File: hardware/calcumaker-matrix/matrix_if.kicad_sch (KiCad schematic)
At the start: 1 part, among them J1 TO MCU (unified SPI FFC)

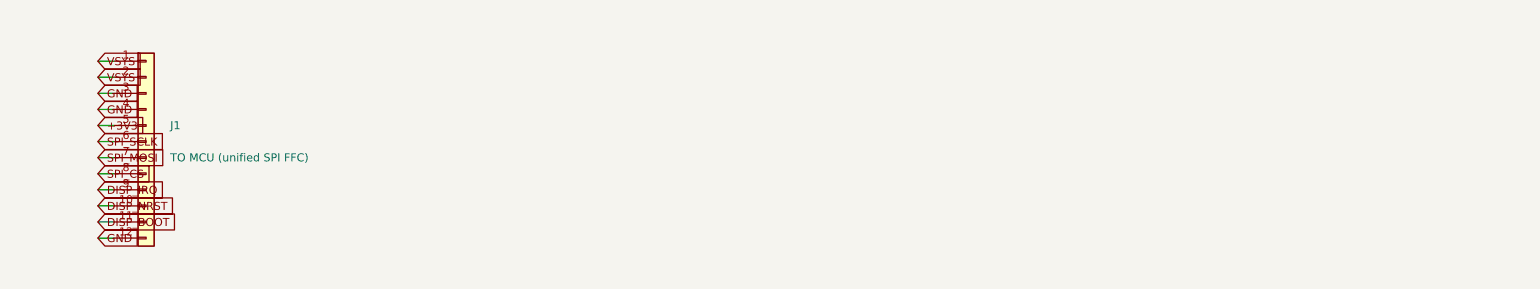
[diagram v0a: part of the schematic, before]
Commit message: Floorplan both display PCBs and verify their schematic nets
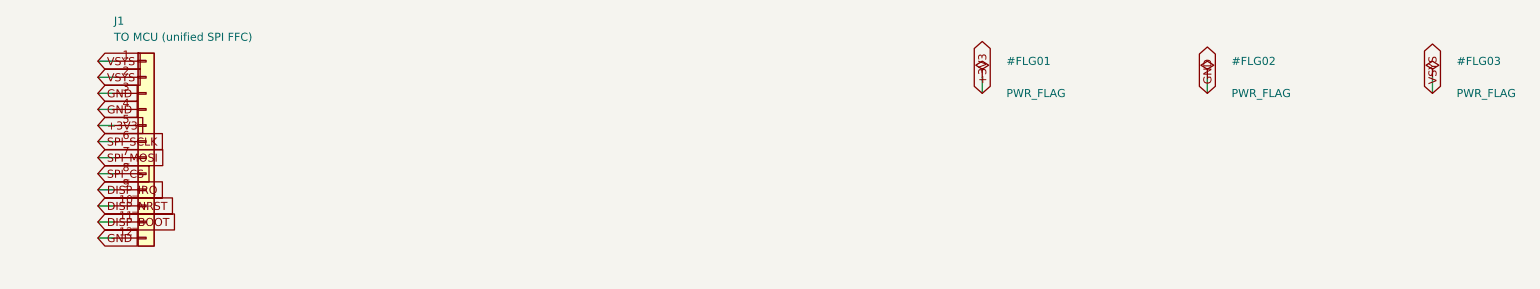
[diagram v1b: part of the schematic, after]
